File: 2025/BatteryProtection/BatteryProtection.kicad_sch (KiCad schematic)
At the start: 43 parts, among them J1 Screw_Terminal_01x02, J2 Screw_Terminal_01x02, Q1 FDMS8333L, Q2 FDMS8333L, Q3 FDMS8333L, Q4 FDMS8333L, U1 MAX25431ATGA/VY+

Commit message: complete circuit
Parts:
- removed C1, C2: 100n, Capacitor_SMD:C_0603_1608Metric, symbol Device:C_Small
- removed C10, C11, C3, C6, C7, C8: 22u, Capacitor_SMD:C_1812_4532Metric, symbol Device:C_Small
- removed C4: 4.7u, Capacitor_SMD:C_1210_3225Metric, symbol Device:C_Small
- removed C5: 36n, Capacitor_SMD:C_0603_1608Metric, symbol Device:C_Small
- removed C9: 120p, Capacitor_SMD:C_0603_1608Metric, symbol Device:C_Small
- removed D1: LED, LED_SMD:LED_0805_2012Metric, symbol Device:LED
- removed D2, D3: DFLS160-7, Diode_SMD:D_SOD-123, symbol Device:D_Small
- removed D4, D5, D6, D7: BAT54XV2T1G, Diode_SMD:D_SOD-523, symbol Device:D_Small
- removed J1, J2: Screw_Terminal_01x02, TerminalBlock_Phoenix:TerminalBlock_Phoenix_MKDS-1,5-2_1x02_P5.00mm_Horizontal, symbol Connector:Screw_Terminal_01x02
- removed L1: 13uH, AllenControlsBuckBoost:L_Wuerth_HCI-1365, symbol Device:L
- removed Q1, Q2, Q3, Q4: FDMS8333L, Package_TO_SOT_SMD:TDSON-8-1, symbol Transistor_FET:FDMS8350L
- removed R1, R2: 6m, Resistor_SMD:R_2010_5025Metric, symbol Device:R_Small_US
- removed R10: 182k, Resistor_SMD:R_0402_1005Metric, symbol Device:R_Small_US
- removed R11, R14, R15, R16: 4.7, Resistor_SMD:R_0603_1608Metric, symbol Device:R_Small_US
- removed R12: 6.19k, Resistor_SMD:R_0402_1005Metric, symbol Device:R_Small_US
- removed R13, R3, R6: 10k, Resistor_SMD:R_0402_1005Metric, symbol Device:R_Small_US
- removed R4: 2.2k, Resistor_SMD:R_0402_1005Metric, symbol Device:R_Small_US
- removed R5, R7: 1, Resistor_SMD:R_0603_1608Metric, symbol Device:R_Small_US
- removed R8: 41.2, Resistor_SMD:R_0402_1005Metric, symbol Device:R_Small_US
- removed R9: 73.2k, Resistor_SMD:R_0402_1005Metric, symbol Device:R_Small_US
- removed TP1: VCC, TestPoint:TestPoint_Pad_1.5x1.5mm, symbol Connector:TestPoint
- removed U1: MAX25431ATGA/VY+, AllenControlsBuckBoost:21-100290_MXM, symbol AllenControlsBuckBoost:MAX25431ATGA_VY+_Functional
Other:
- note removed: "40v"
- note removed: "Connectors"
- note removed: "MAX25431"
- note removed: "Power Good Indicator"
- note removed: "Power Stage"

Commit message: Added components to schematic
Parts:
- added D1: D_Zener, symbol Device:D_Zener
- added Q1: BC849, Package_TO_SOT_SMD:SOT-23, symbol Transistor_BJT:BC849
- added Q2: IXTA140P05T, Package_TO_SOT_SMD:TO-263-2, symbol BatteryProtection:IXTA140P05T
- added U1: PLACEHOLDER, Package_TO_SOT_SMD:SOT-23-5, symbol Comparator:LM397

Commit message: Started on PCB
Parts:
- added C1, C2: 10nF, Capacitor_SMD:C_0603_1608Metric_Pad1.08x0.95mm_HandSolder, symbol Device:C
- added C3, C4: 1uF, Capacitor_SMD:C_0603_1608Metric_Pad1.08x0.95mm_HandSolder, symbol Device:C
- added C5: 0.1uF, Capacitor_SMD:C_0603_1608Metric_Pad1.08x0.95mm_HandSolder, symbol Device:C
- added D2: 5.6V, Diode_SMD:D_0603_1608Metric_Pad1.05x0.95mm_HandSolder, symbol Device:D_Zener
- added Q10, Q11, Q3, Q4, Q5, Q6, Q7, Q8, Q9: BC849, Package_TO_SOT_SMD:SOT-23, symbol Transistor_BJT:BC849
- added R1, R10, R12, R13, R14, R8: 100k, Resistor_SMD:R_0603_1608Metric_Pad0.98x0.95mm_HandSolder, symbol Device:R_US
- added R11: Load, Resistor_SMD:R_0603_1608Metric_Pad0.98x0.95mm_HandSolder, symbol Device:R_US
- added R15, R16, R17, R18, R19, R20, R21, R22, R23, R5, R6, R7, R9: 1k, Resistor_SMD:R_0603_1608Metric_Pad0.98x0.95mm_HandSolder, symbol Device:R_US
- added R2: 50k, Resistor_SMD:R_0603_1608Metric_Pad0.98x0.95mm_HandSolder, symbol Device:R_US
- added R3, R4: 10k, Resistor_SMD:R_0603_1608Metric_Pad0.98x0.95mm_HandSolder, symbol Device:R_US
- added U2: PLACEHOLDER, Package_TO_SOT_SMD:SOT-23-5, symbol Comparator:LM397
- D1: value D_Zener -> 4.7V; footprint (none) -> Diode_SMD:D_0603_1608Metric_Pad1.05x0.95mm_HandSolder
- renumbered Q2 to Q1, Q1 to Q2
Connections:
- net at Q1.1 (G): now also C5.2, R10.1, R9.1
- net Vs: now reaches Q1.2 (D)
- net Vs: now also Q2.3 (C), U1.5 (V+), C3.2, C4.2, Q3.3 (C), Q4.3 (C), R1.1, R10.2, R12.2, R13.2, R14.2, R22.1, R23.1, R3.1, R4.1, U2.5 (V+)
- net at Q1.3 (S): now also R11.2
- net at D1.1 (K): now also C2.1, R4.2, U2.3 (+)
- net GND: now reaches D1.2 (A)
- net GND: now also U1.2 (V-), C1.2, C2.2, C3.1, C4.1, D2.2 (A), Q10.2 (E), Q11.2 (E), Q5.2 (E), Q7.2 (E), Q8.2 (E), Q9.2 (E), R11.1, R2.2, R8.1, U2.2 (V-)
- net at Q2.1 (B): now also R5.1
- net at Q2.2 (E): now also C5.1, Q3.2 (E), Q4.2 (E), R8.2, R9.2
- net at U1.1 (-): now also C1.1, D2.1 (K), R3.2
- net at U1.3 (+): now also R1.2, R2.1, U2.1 (-)
- net at U1.4: now also R5.2
- new net: R6.1, U2.4
- new net: Q3.1 (B), R6.2
- new net: Q9.3 (C), R16.1, R19.1, R22.2
- new net: Q10.1 (B), R19.2
- new net: Q5.3 (C), R12.1, R17.1
- new net: Q11.1 (B), R21.2
- new net: Q10.3 (C), Q11.3 (C), R20.2, R23.2
- new net: Q9.1 (B), R20.1
- new net: Q8.1 (B), R15.2
- new net: Q8.3 (C), R14.1, R7.1
- new net: Q6.3 (C), R13.1, R15.1
- new net: Q5.1 (B), R18.2
- new net: Q6.1 (B), R17.2
- new net: Q4.1 (B), R7.2
- new net: Q7.1 (B), R16.2
- new net: Q6.2 (E), Q7.3 (C)
- new net Gpio: R18.1, R21.1
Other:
- company: Peter Buckley Engineering -> Nathan Oftedal
- title: MAX25431 Buck Boost -> Battery Protection Circuit
- moved on the sheet: D1, Q1, Q2, U1

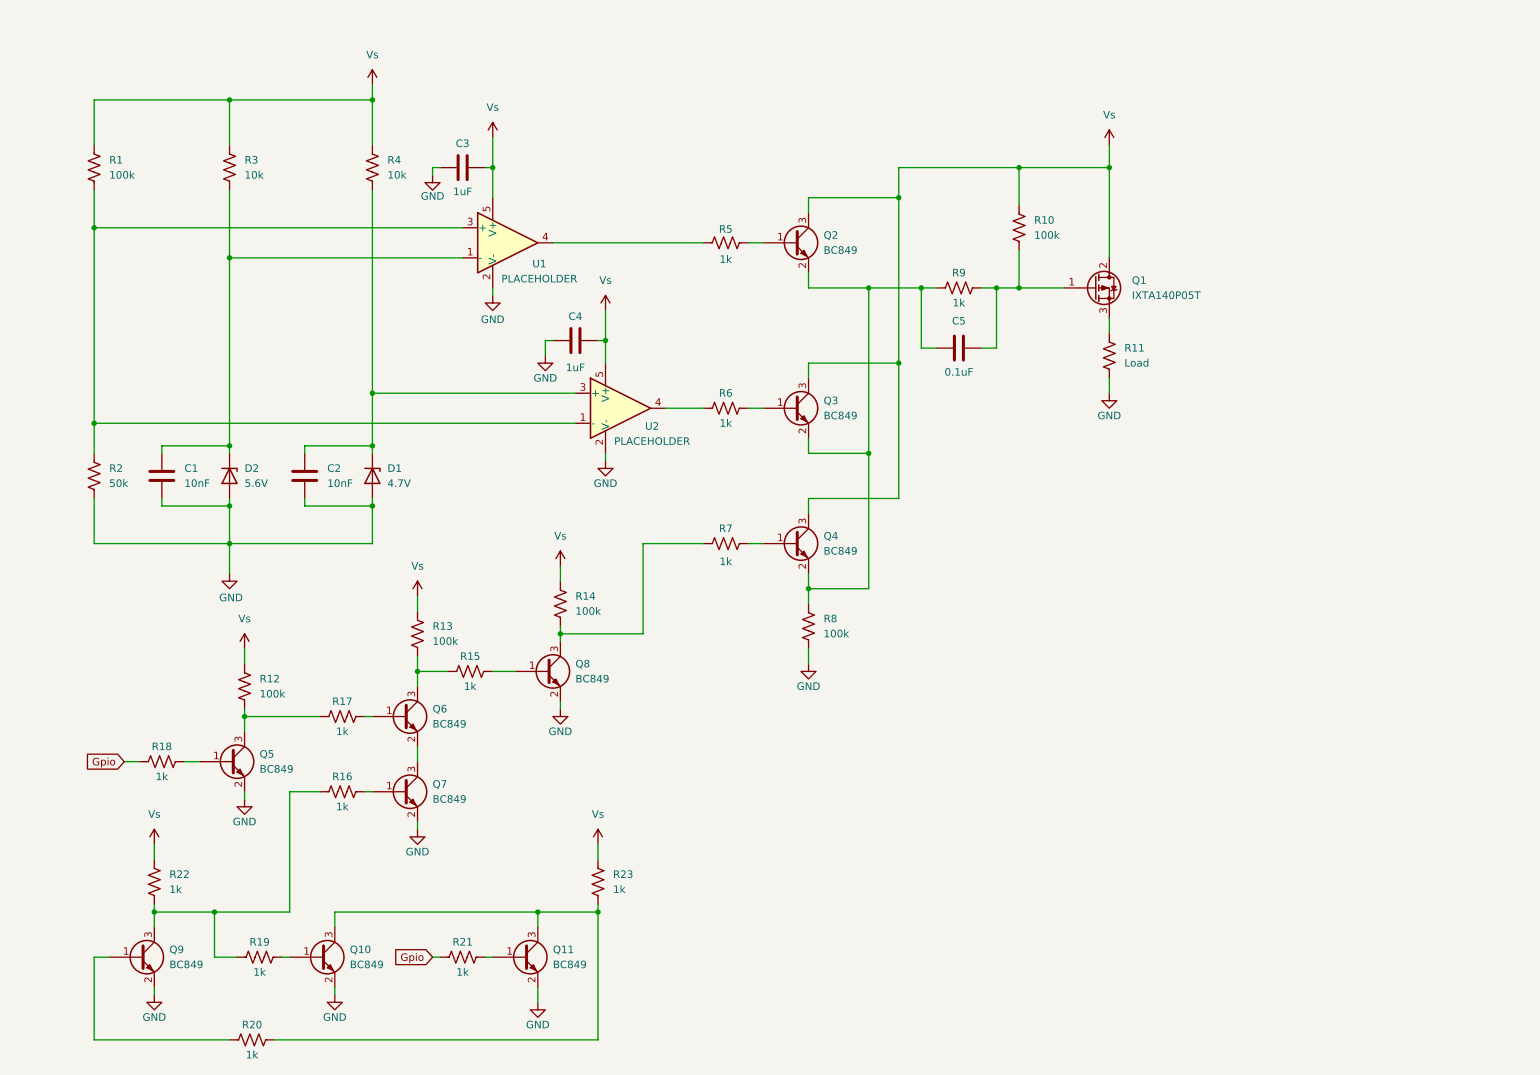
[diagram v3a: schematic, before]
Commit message: Added ldo and comparitors
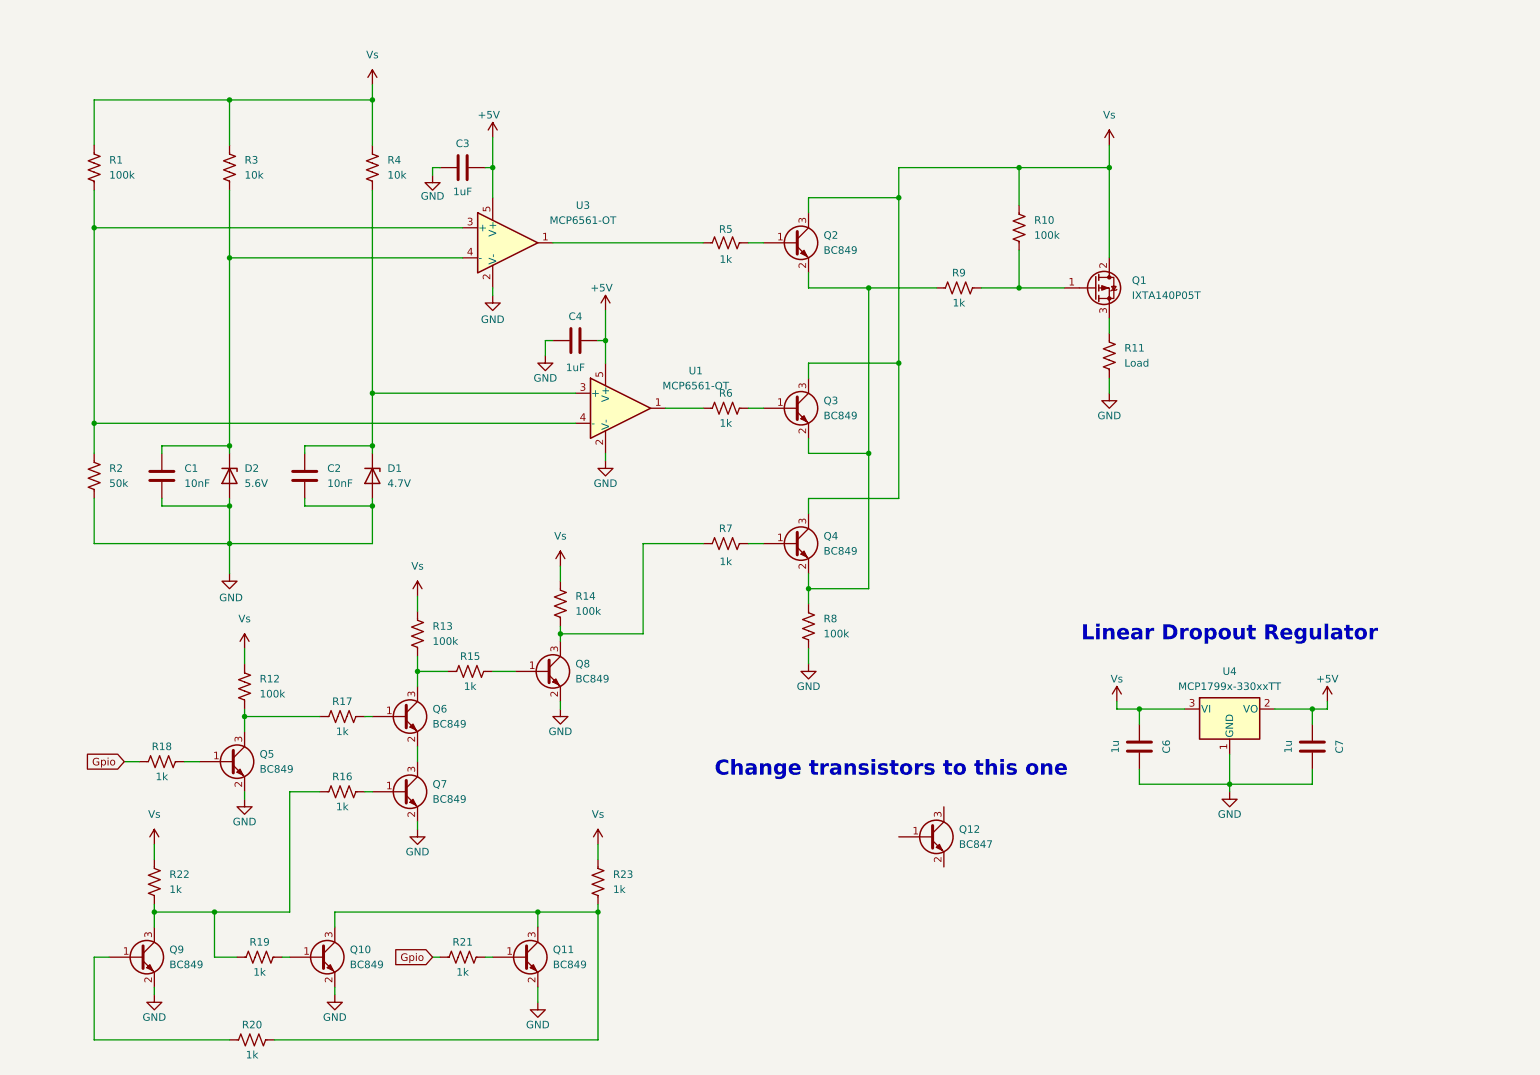
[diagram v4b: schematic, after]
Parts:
- removed C5: 0.1uF, Capacitor_SMD:C_0603_1608Metric_Pad1.08x0.95mm_HandSolder, symbol Device:C
- removed U1, U2: PLACEHOLDER, Package_TO_SOT_SMD:SOT-23-5, symbol Comparator:LM397
- added C6, C7: 1u, Capacitor_SMD:C_0603_1608Metric_Pad1.08x0.95mm_HandSolder, symbol Device:C
- added Q12: BC847, Package_TO_SOT_SMD:SOT-23, symbol Transistor_BJT:BC847
- added U1, U3: MCP6561-OT, Package_TO_SOT_SMD:SOT-23-5, symbol Comparator:MCP6561-OT
- added U4: MCP1799x-330xxTT, Package_TO_SOT_SMD:SOT-23, symbol Regulator_Linear:MCP1799x-330xxTT
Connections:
- net GND: now also C6.2, C7.2, U1.2 (V-), U3.2 (V-), U4.1 (GND)
- net Vs: now also C6.1, U4.3 (VI); no longer C3.2, C4.2
- net at R6.1: now also U1.1
- net at C2.1, D1.1 (K), R4.2: now also U1.3 (+)
- net at C1.1, D2.1 (K), R3.2: now also U3.4 (-)
- net at R1.2, R2.1: now also U1.4 (-), U3.3 (+)
- net at R5.2: now also U3.1
- new net +5V: C3.2, C4.2, C7.1, U1.5 (V+), U3.5 (V+), U4.2 (VO)
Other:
- note added: "Change transistors to this one"
- note added: "Linear Dropout Regulator"

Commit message: Added connectors
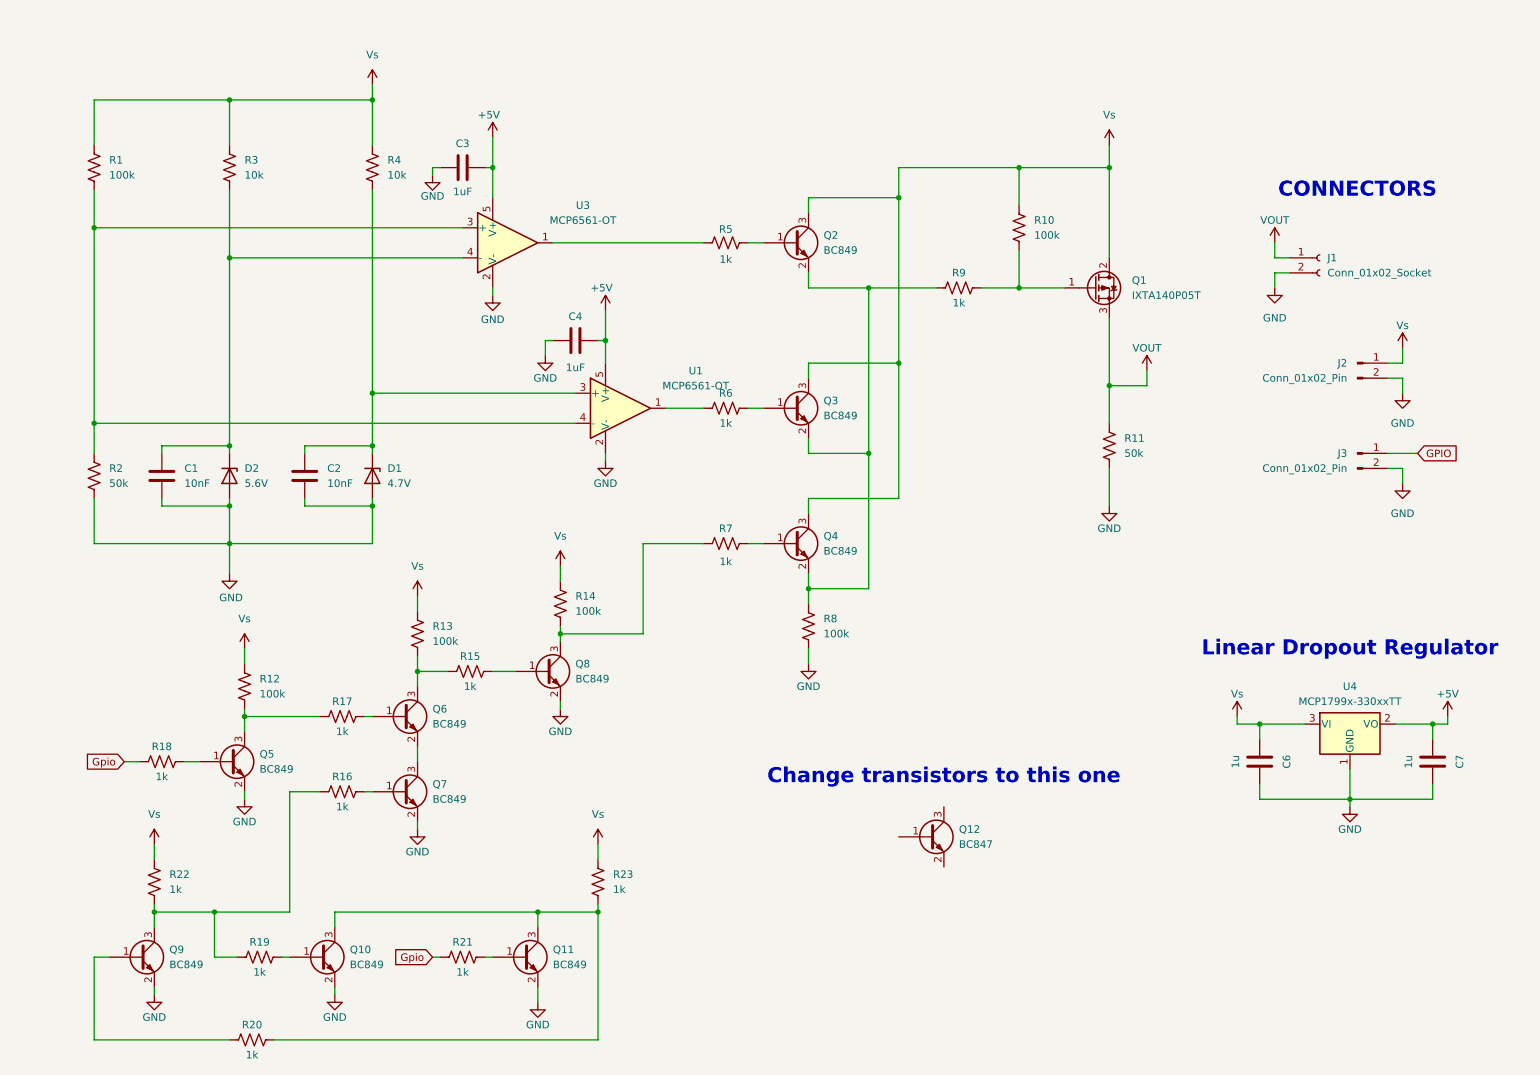
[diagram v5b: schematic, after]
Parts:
- added J1: Conn_01x02_Socket, Connector_JST:JST_XH_B2B-XH-A_1x02_P2.50mm_Vertical, symbol Connector:Conn_01x02_Socket
- added J2: Conn_01x02_Pin, BatteryProtection:XT90PW-M, symbol Connector:Conn_01x02_Pin
- added J3: Conn_01x02_Pin, BatteryProtection:XT90PW-F, symbol Connector:Conn_01x02_Pin
- R11: value Load -> 50k
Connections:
- net GND: now also J1.2 (Pin_2), J2.2 (Pin_2), J3.2 (Pin_2)
- net Vs: now also J2.1 (Pin_1)
- net VOUT: now reaches Q1.3 (S), R11.2
- net VOUT: now also J1.1 (Pin_1)
- new net GPIO: J3.1 (Pin_1)
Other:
- note added: "CONNECTORS"
- moved on the sheet: C6, C7, R11, U4

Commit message: changed transistors
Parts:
- Q10, Q11, Q2, Q3, Q4, Q5, Q6, Q7, Q8, Q9: value BC849 -> BC847; symbol Transistor_BJT:BC849 -> Transistor_BJT:BC847
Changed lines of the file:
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@@
 	)
 	(symbol
-		(lib_id "Transistor_BJT:BC849")
+		(lib_id "Transistor_BJT:BC847")
 		(at 77.47 175.26 0)
 		(unit 1)
@@
 			)
 		)
-		(property "Value" "BC849"
+		(property "Value" "BC847"
 			(at 82.55 176.5299 0)
 			(effects
@@
 			)
 		)
-		(property "Description" "0.1A Ic, 30V Vce, NPN Transistor, SOT-23"
+		(property "Description" "0.1A Ic, 45V Vce, NPN Transistor, SOT-23"
 			(at 77.47 175.26 0)
 			(effects
@@
 	)
 	(symbol
-		(lib_id "Transistor_BJT:BC849")
+		(lib_id "Transistor_BJT:BC847")
 		(at 115.57 127 0)
 		(unit 1)
@@
 			)
 		)
-		(property "Value" "BC849"
+		(property "Value" "BC847"
 			(at 120.65 128.2699 0)
 			(effects
@@
 			)
 		)
-		(property "Description" "0.1A Ic, 30V Vce, NPN Transistor, SOT-23"
+		(property "Description" "0.1A Ic, 45V Vce, NPN Transistor, SOT-23"
 			(at 115.57 127 0)
 			(effects
@@
 	)
 	(symbol
-		(lib_id "Transistor_BJT:BC849")
+		(lib_id "Transistor_BJT:BC847")
 		(at 157.48 54.61 0)
 		(unit 1)
@@
 			)
 		)
-		(property "Value" "BC849"
+		(property "Value" "BC847"
 			(at 162.56 55.8799 0)
 			(effects
@@
 			)
 		)
-		(property "Description" "0.1A Ic, 30V Vce, NPN Transistor, SOT-23"
+		(property "Description" "0.1A Ic, 45V Vce, NPN Transistor, SOT-23"
 			(at 157.48 54.61 0)
 			(effects
@@
 	)
 	(symbol
-		(lib_id "Transistor_BJT:BC849")
+		(lib_id "Transistor_BJT:BC847")
 		(at 62.23 142.24 0)
 		(unit 1)
@@
 			)
 		)
-		(property "Value" "BC849"
+		(property "Value" "BC847"
 			(at 67.31 143.5099 0)
 			(effects
@@
 			)
 		)
-		(property "Description" "0.1A Ic, 30V Vce, NPN Transistor, SOT-23"
+		(property "Description" "0.1A Ic, 45V Vce, NPN Transistor, SOT-23"
 			(at 62.23 142.24 0)
 			(effects
@@
 	)
 	(symbol
-		(lib_id "Transistor_BJT:BC849")
+		(lib_id "Transistor_BJT:BC847")
 		(at 46.99 175.26 0)
 		(unit 1)
@@
 			)
 		)
-		(property "Value" "BC849"
+		(property "Value" "BC847"
 			(at 52.07 176.5299 0)
 			(effects
@@
 			)
 		)
-		(property "Description" "0.1A Ic, 30V Vce, NPN Transistor, SOT-23"
+		(property "Description" "0.1A Ic, 45V Vce, NPN Transistor, SOT-23"
 			(at 46.99 175.26 0)
 			(effects
@@
 	)
 	(symbol
-		(lib_id "Transistor_BJT:BC849")
+		(lib_id "Transistor_BJT:BC847")
 		(at 91.44 134.62 0)
 		(unit 1)
@@
 			)
 		)
-		(property "Value" "BC849"
+		(property "Value" "BC847"
 			(at 96.52 135.8899 0)
 			(effects
@@
 			)
 		)
-		(property "Description" "0.1A Ic, 30V Vce, NPN Transistor, SOT-23"
+		(property "Description" "0.1A Ic, 45V Vce, NPN Transistor, SOT-23"
 			(at 91.44 134.62 0)
 			(effects
@@
 	)
 	(symbol
-		(lib_id "Transistor_BJT:BC849")
+		(lib_id "Transistor_BJT:BC847")
 		(at 157.48 105.41 0)
 		(unit 1)
@@
 			)
 		)
-		(property "Value" "BC849"
+		(property "Value" "BC847"
 			(at 162.56 106.6799 0)
 			(effects
@@
 			)
 		)
-		(property "Description" "0.1A Ic, 30V Vce, NPN Transistor, SOT-23"
+		(property "Description" "0.1A Ic, 45V Vce, NPN Transistor, SOT-23"
 			(at 157.48 105.41 0)
 			(effects
@@
 	)
 	(symbol
-		(lib_id "Transistor_BJT:BC849")
+		(lib_id "Transistor_BJT:BC847")
 		(at 111.76 175.26 0)
 		(unit 1)
@@
 			)
 		)
-		(property "Value" "BC849"
+		(property "Value" "BC847"
 			(at 116.84 176.5299 0)
 			(effects
@@
 			)
 		)
-		(property "Description" "0.1A Ic, 30V Vce, NPN Transistor, SOT-23"
+		(property "Description" "0.1A Ic, 45V Vce, NPN Transistor, SOT-23"
 			(at 111.76 175.26 0)
 			(effects
@@
 	)
 	(symbol
-		(lib_id "Transistor_BJT:BC849")
+		(lib_id "Transistor_BJT:BC847")
 		(at 157.48 82.55 0)
 		(unit 1)
@@
 			)
 		)
-		(property "Value" "BC849"
+		(property "Value" "BC847"
 			(at 162.56 83.8199 0)
 			(effects
@@
 			)
 		)
-		(property "Description" "0.1A Ic, 30V Vce, NPN Transistor, SOT-23"
+		(property "Description" "0.1A Ic, 45V Vce, NPN Transistor, SOT-23"
 			(at 157.48 82.55 0)
 			(effects
@@
 	)
 	(symbol
-		(lib_id "Transistor_BJT:BC849")
+		(lib_id "Transistor_BJT:BC847")
 		(at 91.44 147.32 0)
 		(unit 1)
@@
 			)
 		)
-		(property "Value" "BC849"
+		(property "Value" "BC847"
 			(at 96.52 148.5899 0)
 			(effects
@@
 			)
 		)
-		(property "Description" "0.1A Ic, 30V Vce, NPN Transistor, SOT-23"
+		(property "Description" "0.1A Ic, 45V Vce, NPN Transistor, SOT-23"
 			(at 91.44 147.32 0)
 			(effects
